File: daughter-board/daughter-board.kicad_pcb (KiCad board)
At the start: 2 copper layers, 27 x 16.5 mm, 10 parts, among them J1 USB_C_Receptacle_USB2.0_16P, J2 Conn_01x06_MountingPin

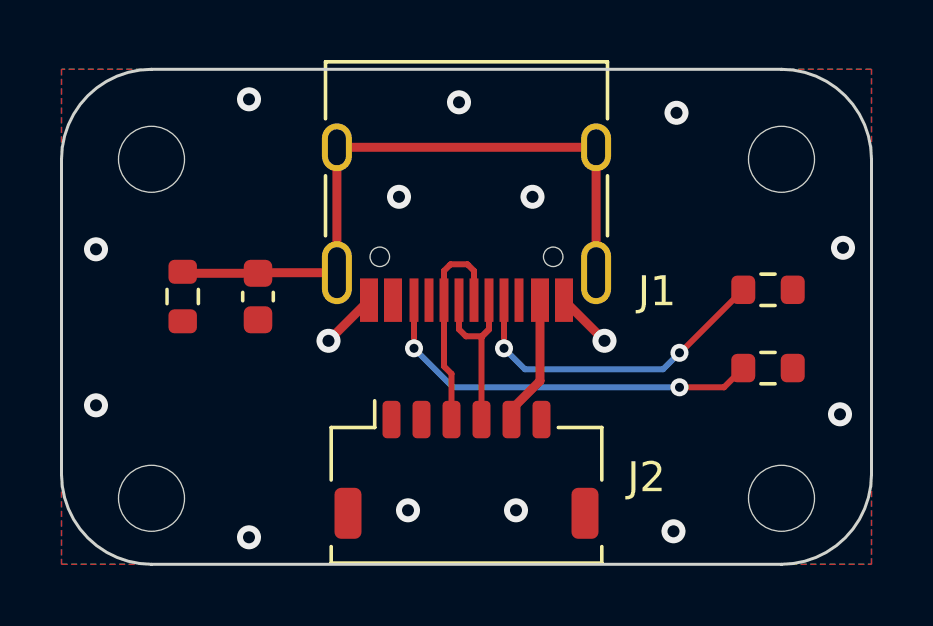
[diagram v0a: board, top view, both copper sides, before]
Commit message: updated findings from prototype removed output folder as the vendors stock is everchanging
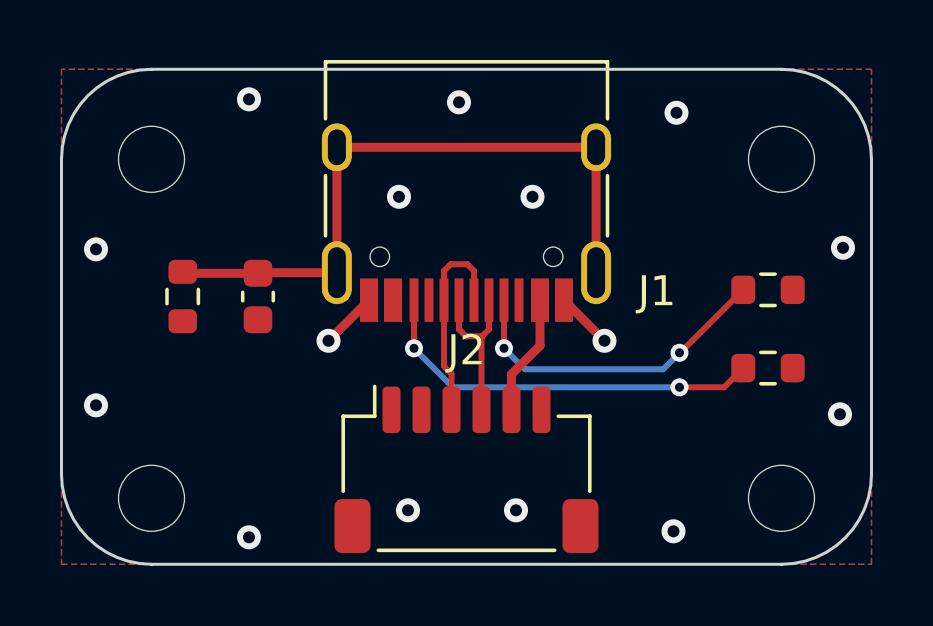
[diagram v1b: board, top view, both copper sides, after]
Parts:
- J2: footprint Connector_JST:JST_SHL_SM06B-SHLS-TF_1x06-1MP_P1.00mm_Horizontal -> Connector_JST:JST_SH_SM06B-SRSS-TB_1x06-1MP_P1.00mm_Horizontal
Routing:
- net /USB_D-: track 6.25 -> 5.60 mm
